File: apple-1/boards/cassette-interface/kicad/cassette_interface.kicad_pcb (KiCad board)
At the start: 2 copper layers, 102.6 x 50.7 mm, 23 parts, among them J1 APPLE1_EDGE, J2 audio_jack, J3 audio_jack, Q1 Q_NPN_EBC, Q2 Q_NPN_EBC, U1 74LS02, U2 74LS10, U3 LM311, U4 74LS74, U5 MMI6301, U6 MMI6301

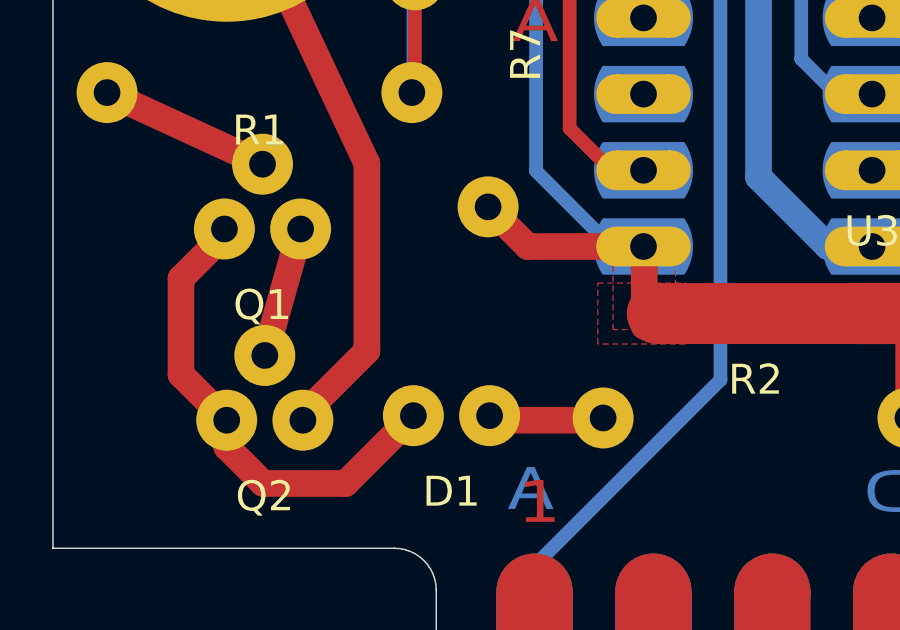
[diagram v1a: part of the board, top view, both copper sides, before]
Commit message: add polarity mark for LED1
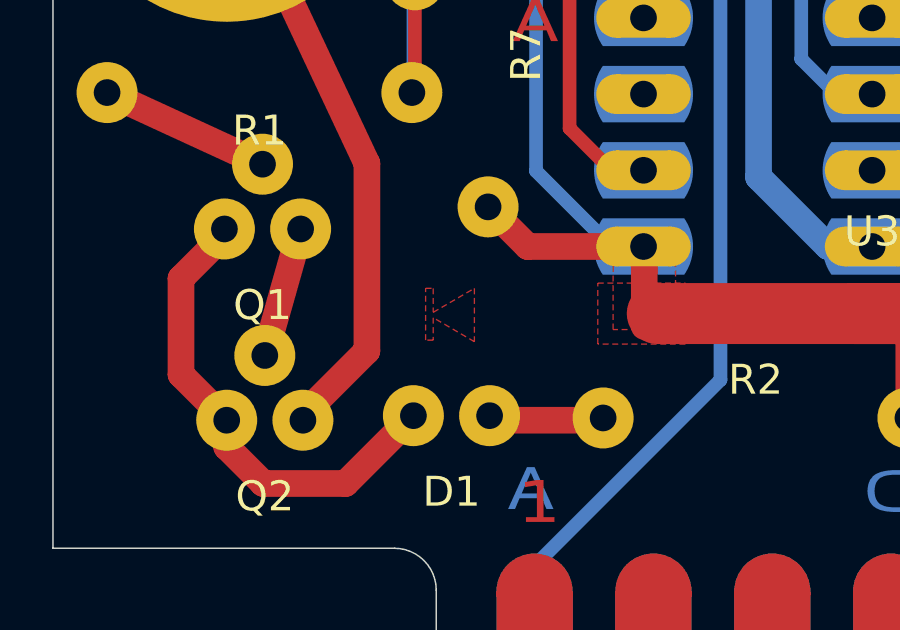
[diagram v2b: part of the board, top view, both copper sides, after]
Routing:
- added copper zone on F.Cu, net (none)
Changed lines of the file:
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@@
     (user_trace_width 2.54)
     (trace_clearance 0.2032)
-    (zone_clearance 0.3048)
+    (zone_clearance 0.1016)
     (zone_45_only no)
     (trace_min 0.3048)
@@
       )
     )
+  )
+  (zone (net 0) (net_name "") (layer F.Cu) (hatch edge 0.508)
+    (connect_pads (clearance 0.1016))
+    (min_thickness 0.1016)
+    (fill yes (arc_segments 32) (thermal_gap 0.508) (thermal_bridge_width 0.508))
+    (polygon
+      (pts
+        (xy 114.275498 109.052259) (xy 115.647098 108.252159) (xy 115.647098 110.030159) (xy 114.275498 109.230059) (xy 114.275498 109.979359)
+        (xy 114.021498 109.979359) (xy 114.021498 108.252159) (xy 114.275498 108.252159)
+      )
+    )

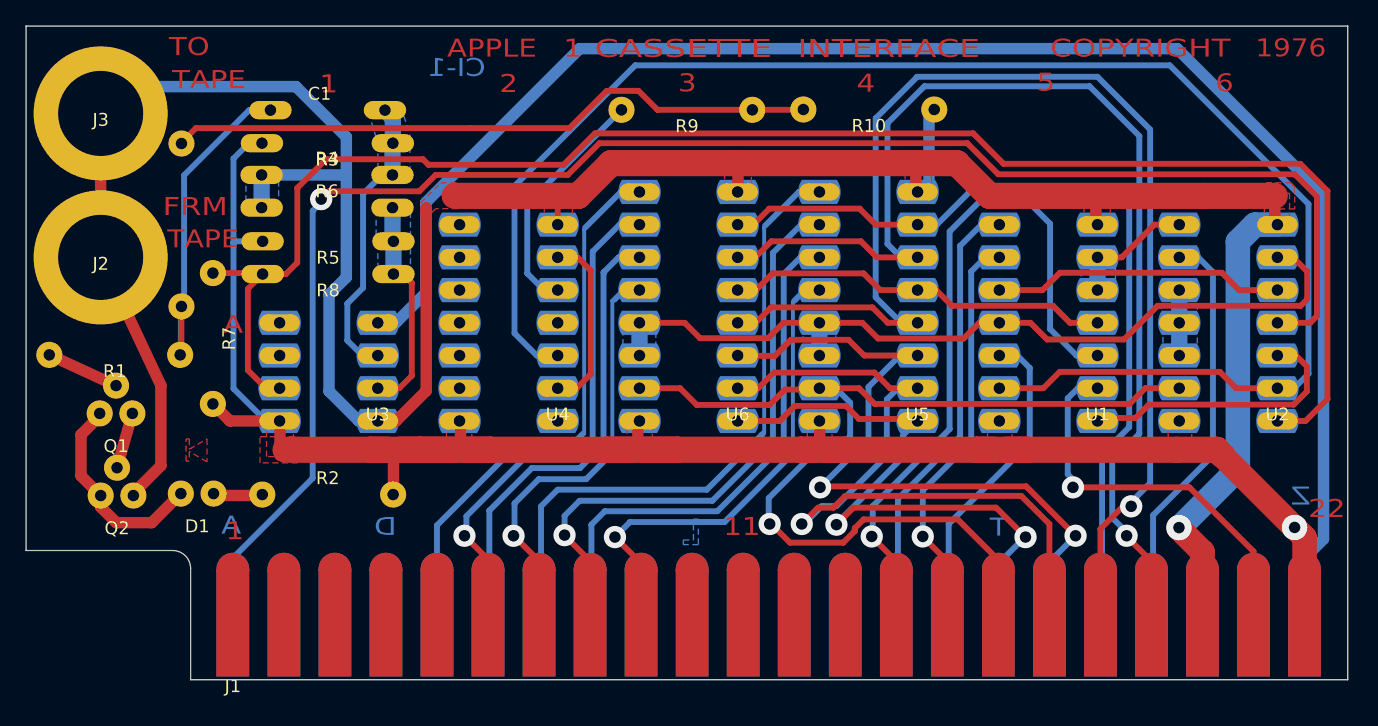
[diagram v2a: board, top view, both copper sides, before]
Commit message: small layout tweaks for accuracy; use gerber X2; remove NPTH since there are none
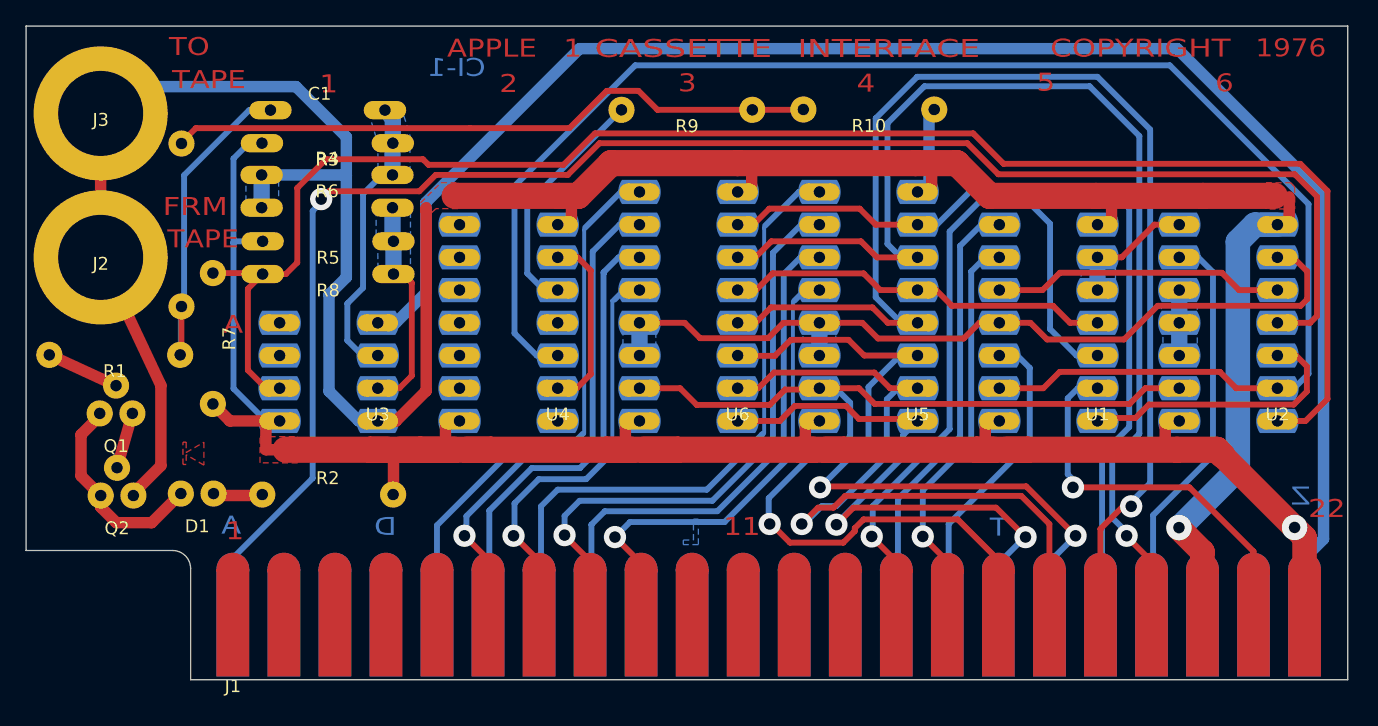
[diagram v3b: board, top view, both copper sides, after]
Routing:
- net +5V: track 153.9 -> 162.5 mm
- net GND: track 232.0 -> 237.4 mm
